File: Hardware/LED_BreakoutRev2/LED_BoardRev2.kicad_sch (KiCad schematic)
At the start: 35 parts, among them Q1 BSS214NW, Q2 BSS214NW, Q3 BSS214NW, Q4 BSS214NW, Q5 BSS214NW, Q6 BSS214NW

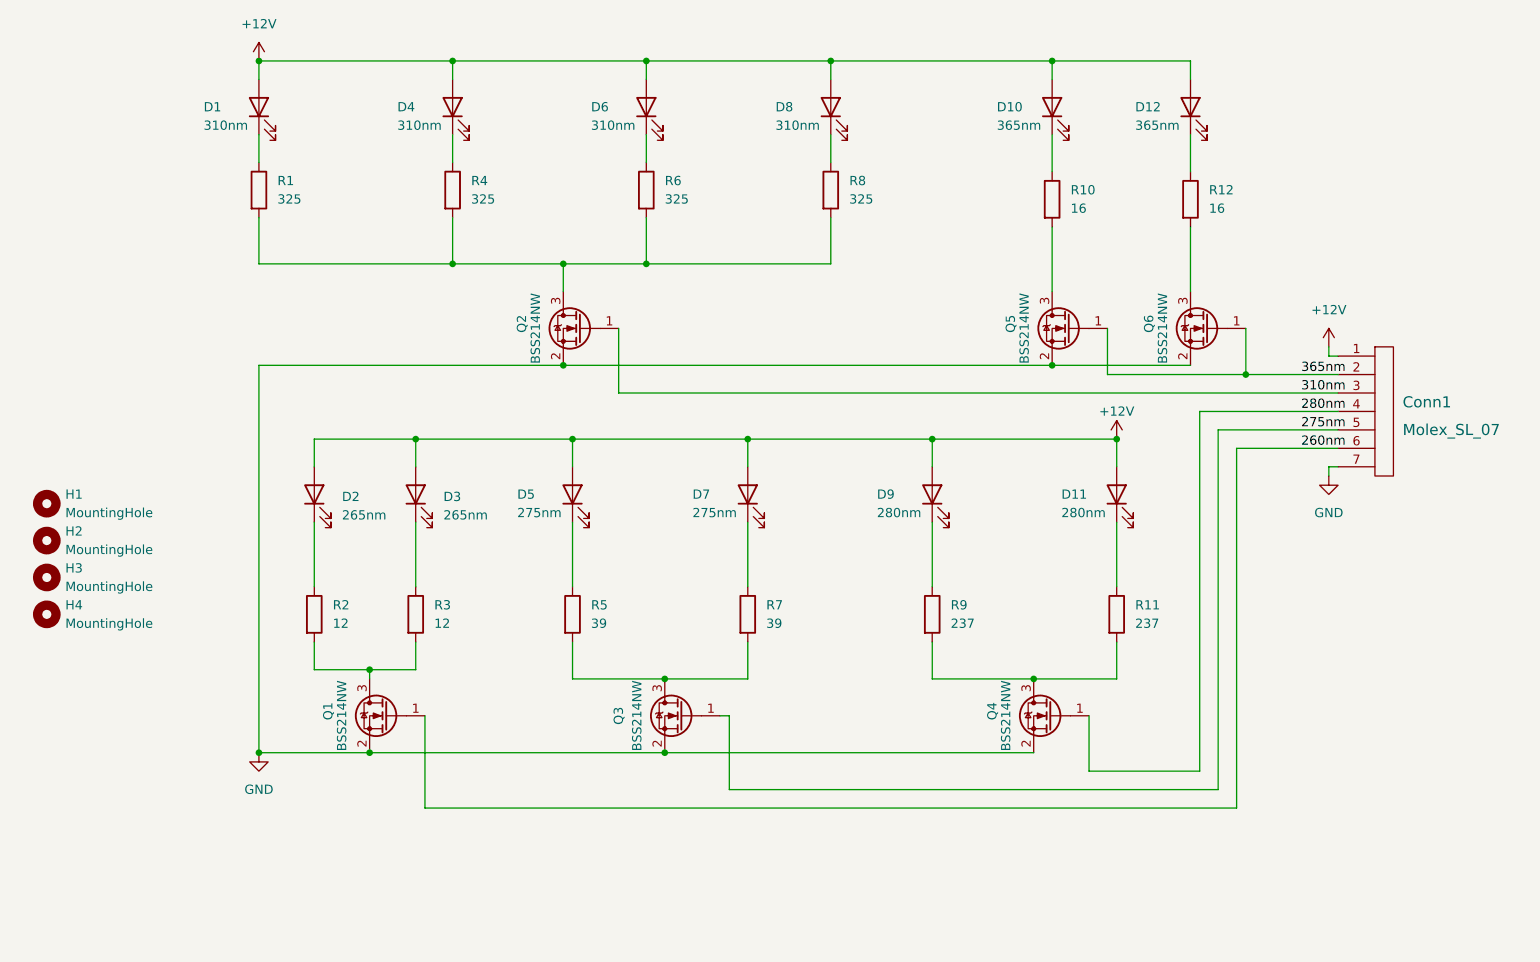
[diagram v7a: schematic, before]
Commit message: Finished LED Board Rev2
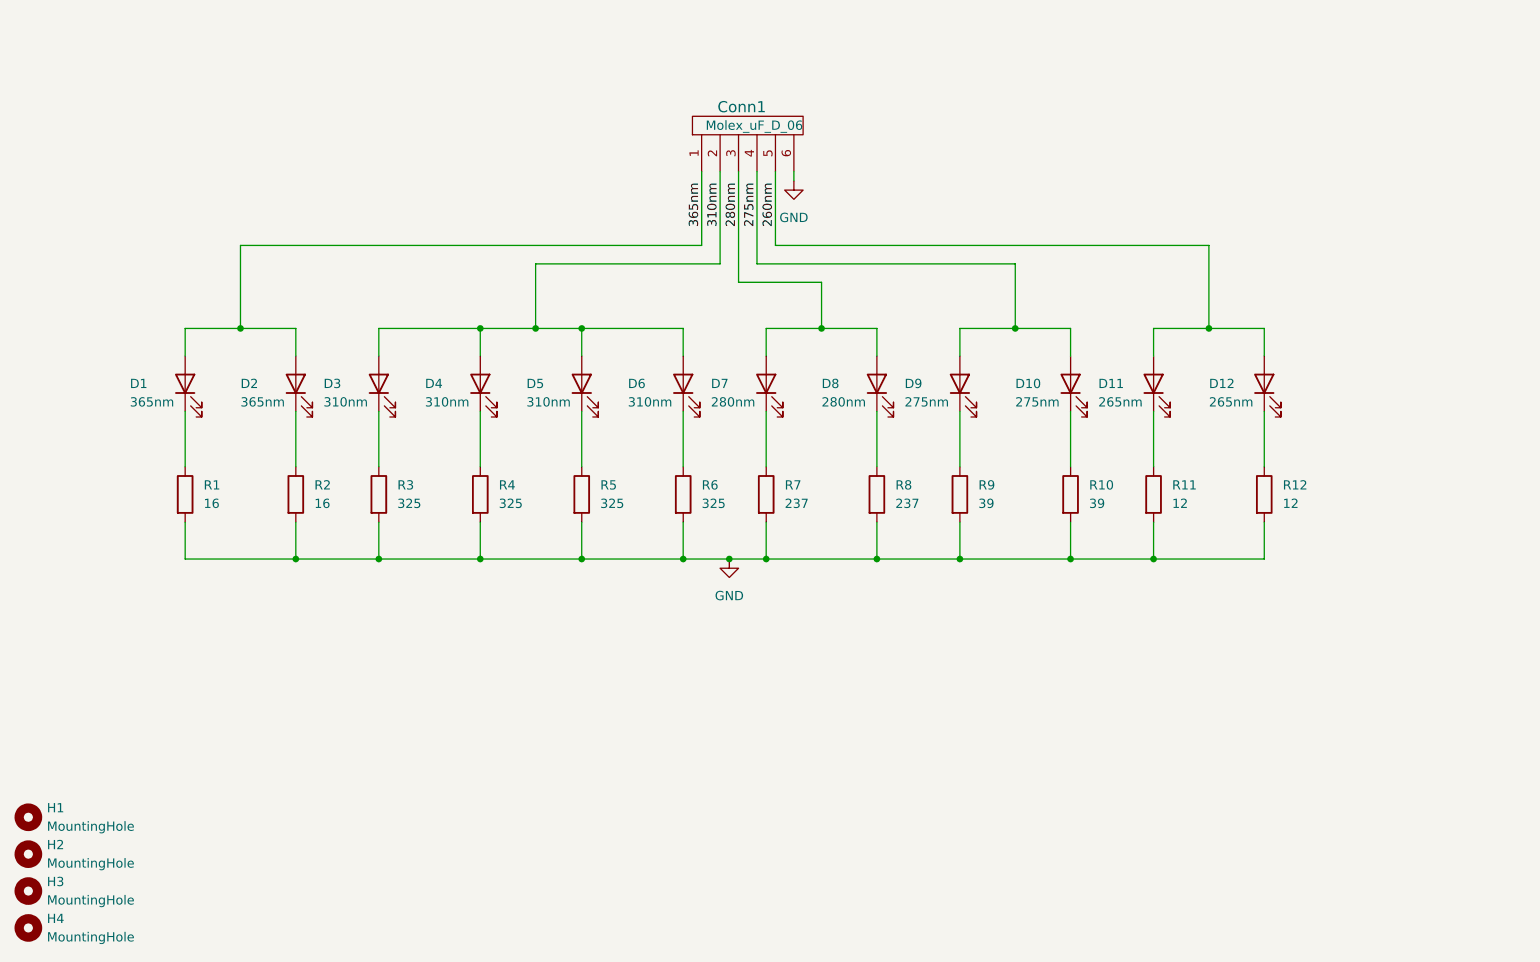
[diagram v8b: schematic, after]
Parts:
- removed Conn1: Molex_SL_07, MRDT_Connectors:MOLEX_SL_07_Vertical, symbol MRDT_Connectors:Molex_SL_07
- removed Q1, Q2, Q3, Q4, Q5, Q6: BSS214NW, Package_TO_SOT_SMD:SOT-323_SC-70, symbol Transistor_FET:BSS214NW
- added Conn1: Molex_uF_D_06, Connector_Molex:Molex_SL_171971-0006_1x06_P2.54mm_Vertical, symbol MRDT_Connectors:Molex_uF_D_06
- renumbered D10 to D1, D7 to D10, D2 to D11, D3 to D12, D12 to D2, D1 to D3, D6 to D5, D8 to D6, D9 to D7, D11 to D8, D5 to D9, R10 to R1, R7 to R10, R2 to R11, R3 to R12, R12 to R2, R1 to R3, R6 to R5, R8 to R6, R9 to R7, R11 to R8, R5 to R9
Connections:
- net 260nm: now also D11.2 (A), D12.2 (A), Conn1.5
- net 275nm: now also D10.2 (A), D9.2 (A), Conn1.4
- net 280nm: now also D7.2 (A), D8.2 (A), Conn1.3
- net 310nm: now also D3.2 (A), D4.2 (A), D5.2 (A), D6.2 (A), Conn1.2
- net 365nm: now also D1.2 (A), D2.2 (A), Conn1.1
- net GND: now also R1.2, R10.2, R11.2, R12.2, R2.2, R3.2, R4.2, R5.2, R6.2, R7.2, R8.2, R9.2, Conn1.6
- removed net +12V: D1.2 (A), D10.2 (A), D11.2 (A), D12.2 (A), D2.2 (A), D3.2 (A), D4.2 (A), D5.2 (A), D6.2 (A), D7.2 (A), D8.2 (A), D9.2 (A)
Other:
- moved on the sheet: D1, D10, D11, D12, D2, D3, D4, D5, D6, D7, D8, D9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
